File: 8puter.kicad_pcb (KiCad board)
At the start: 2 copper layers, 100 x 100 mm, 95 parts, among them J1 PWR-DC, U1 74AC00, U2 74AHC74, U3 74HC126, U6 MAX811TEUS+T, X1 ECS-2200BX-100

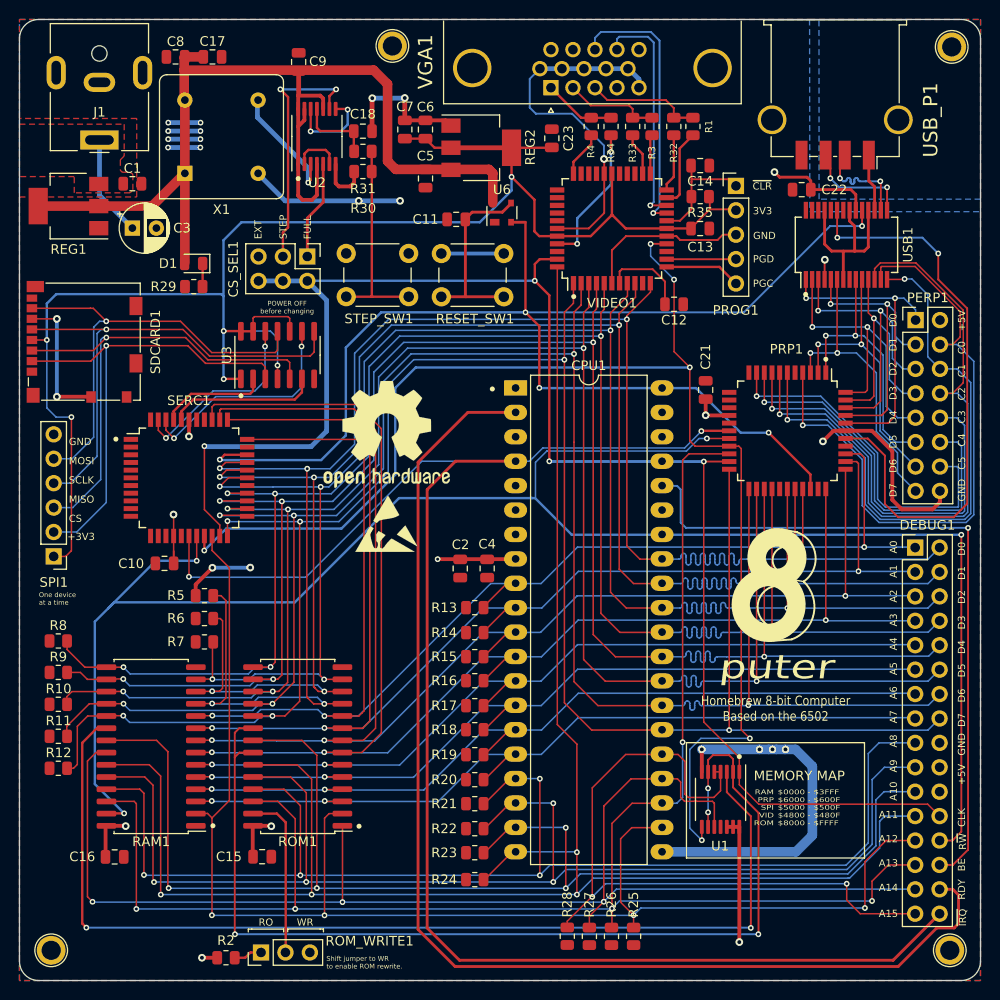
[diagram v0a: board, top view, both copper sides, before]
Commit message: Comments in Sch
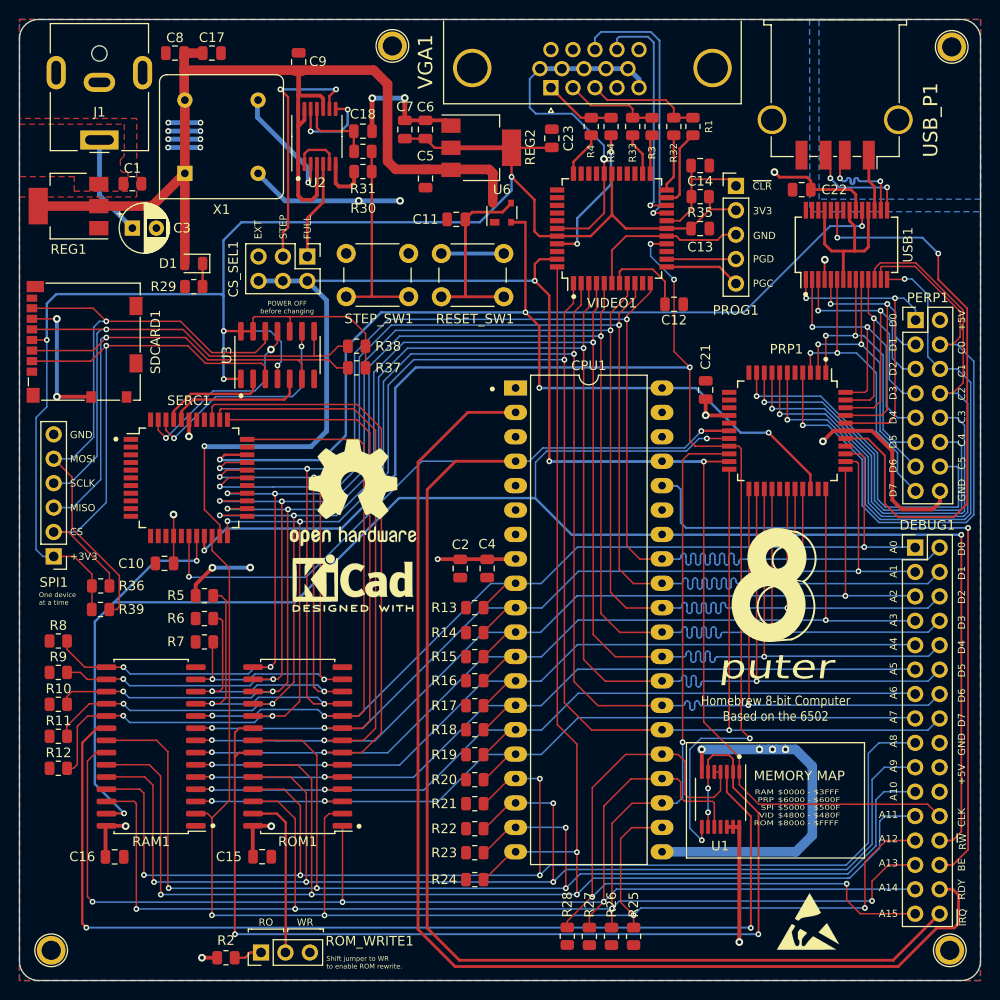
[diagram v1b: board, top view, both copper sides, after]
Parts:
- added R36: 1K, Resistor_SMD:R_0805_2012Metric, F.Cu at (113.0, 94.0)
- added R37: 1K, Resistor_SMD:R_0805_2012Metric, F.Cu at (139.7, 71.3)
- added R38: 1K, Resistor_SMD:R_0805_2012Metric, F.Cu at (139.7, 69.1)
- added R39: 1K, Resistor_SMD:R_0805_2012Metric, F.Cu at (113.0, 96.5)
- added REF**: KiCad-Logo2_5mm_SilkScreen, Symbol:KiCad-Logo2_5mm_SilkScreen, F.Cu at (139.3, 93.7)
- moved REF** 60.3 mm to (186.7, 128.9)
- moved REF** 7.02 mm to (139.3, 84.3)
- moved C17 0.40 mm to (124.6, 38.6)
- moved C8 0.40 mm to (120.8, 38.6)
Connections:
- SDCARD1 pad 3: /Storage/MISO -> /Storage/MOSI
- SDCARD1 pad 7: /Storage/MOSI -> /Storage/MISO
- SPI1 pad 3: /Storage/MISO -> /Storage/MOSI
- SPI1 pad 5: /Storage/MOSI -> /Storage/MISO
- U3 pad 11: /Storage/MOSI -> Net-(SERC1-Pad43)
- U3 pad 12: Net-(SERC1-Pad43) -> /Storage/MISO
- U3 pad 5: /Storage/MISO -> Net-(SERC1-Pad40)
- U3 pad 6: Net-(SERC1-Pad40) -> /Storage/MOSI
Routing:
- net +3V3: track 174.4 -> 193.9 mm, vias 6 -> 5
- net /Storage/MISO: track 51.5 -> 65.4 mm
- net /Storage/MOSI: track 47.6 -> 58.2 mm
- net /Storage/CS: track 50.2 -> 59.1 mm
- net /Storage/SCLK: track 52.5 -> 56.6 mm
- net +5V: track 166.4 -> 165.1 mm
- net Net-(SERC1-Pad40): track 15.6 -> 14.5 mm
- net Net-(SERC1-Pad43): track 20.2 -> 20.8 mm

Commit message: nicer label
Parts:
- added kibuzzard-628A97D6: G***, kibuzzard-628A97D6, F.Cu at (183.3, 102.5)
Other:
- board text removed: "puter"

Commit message: improve routing
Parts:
- removed the REF** at (186.7, 128.9)
- removed kibuzzard-628A97D6: G***, kibuzzard-628A97D6
- added kibuzzard-628B4C0E: G***, kibuzzard-628B4C0E, B.Cu at (199.7, 45.5)
- added kibuzzard-628B4C0E: G***, kibuzzard-628B4C0E, B.Cu at (132.3, 51.1)
- added kibuzzard-628B4C0E: G***, kibuzzard-628B4C0E, B.Cu at (174.8, 121.7)
- added kibuzzard-628B4D67: G***, kibuzzard-628B4D67, F.Cu at (141.9, 66.2)
- added kibuzzard-628B4DA2: G***, kibuzzard-628B4DA2, F.Cu at (151.8, 66.2)
- added kibuzzard-628B4EC0: G***, kibuzzard-628B4EC0, B.Cu at (158.5, 64.0)
- added kibuzzard-628B4F23: G***, kibuzzard-628B4F23, B.Cu at (182.1, 55.0)
- added kibuzzard-628B4F43: G***, kibuzzard-628B4F43, B.Cu at (159.2, 91.2)
- added kibuzzard-628B4F86: G***, kibuzzard-628B4F86, B.Cu at (127.2, 132.2)
- added kibuzzard-628B4F86: G***, kibuzzard-628B4F86, B.Cu at (168.5, 78.5)
- added kibuzzard-628B50D2: G***, kibuzzard-628B50D2, F.Cu at (183.2, 102.4)
- added kibuzzard-628B5292: G***, kibuzzard-628B5292, F.Cu at (140.9, 130.5)
- moved REF** 1.28 mm to (138.0, 93.7)
- moved REF** 1.28 mm to (138.0, 84.3)
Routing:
- net CPU_R~{W}: track 192.5 -> 186.5 mm
- net /Clock/STEP: track 26.1 -> 24.3 mm
- net ~{IRQ}: track 179.5 -> 180.2 mm
